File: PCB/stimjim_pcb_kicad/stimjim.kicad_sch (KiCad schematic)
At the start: 41 parts, among them J1 Conn_02x08_Odd_Even, J10 USB4105-GF-A, J11 BM03B-SRSS-TB, J4 10129383-910002ALF, SW1 400MSP1R6BLKM6QE, U151 AP2112K-3.3

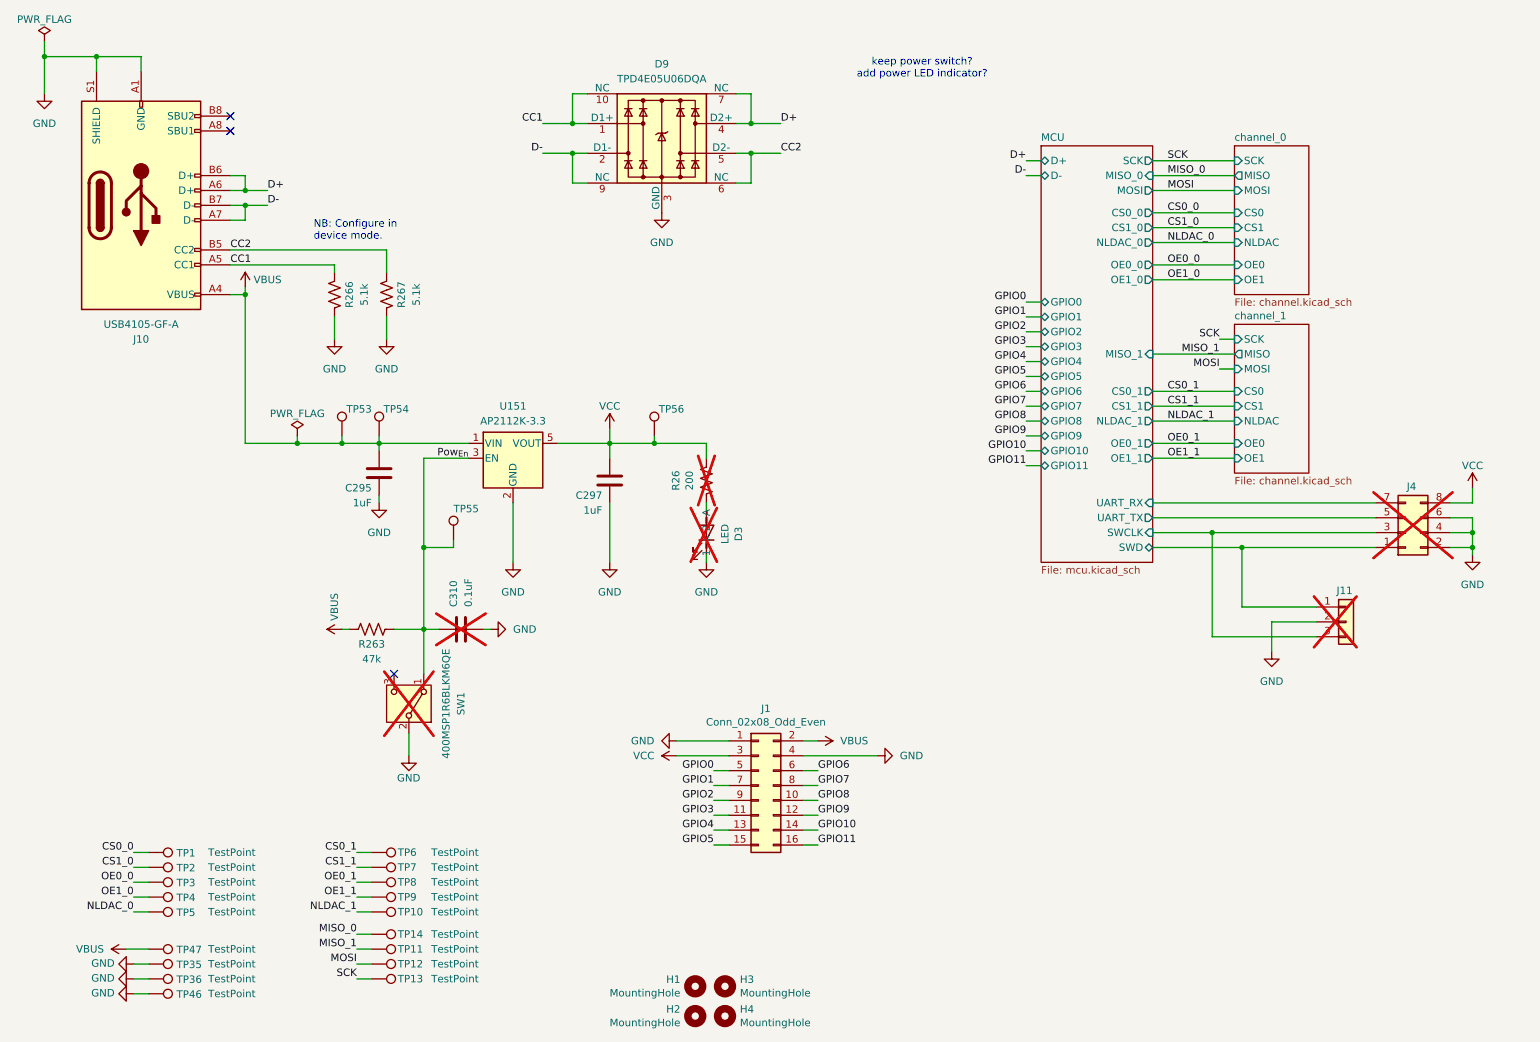
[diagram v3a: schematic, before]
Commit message: Simplified layout
- Went to 4 layers
- Simplified GPIO interface and remove power connections since they are
  a recipe for disaster
- Independent SPI busses to each stimulator to allow simultaneous
  control
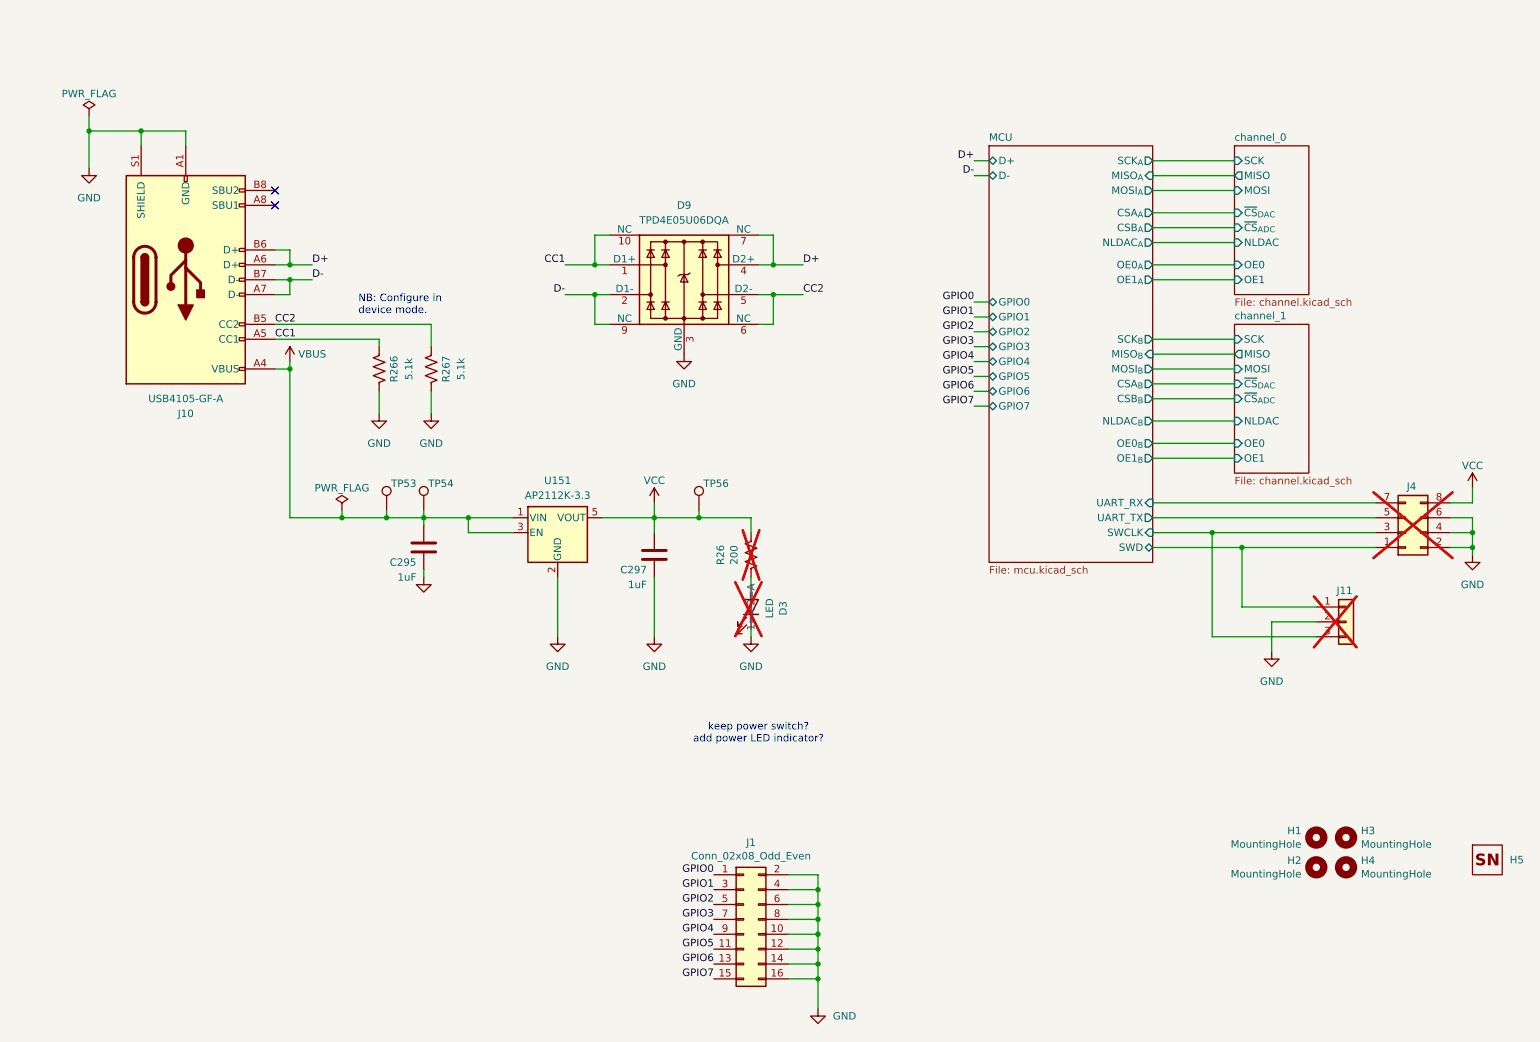
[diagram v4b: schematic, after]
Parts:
- removed C310: 0.1uF, Capacitor_SMD:C_0402_1005Metric, symbol Device:C
- removed R263: 47k, Resistor_SMD:R_0402_1005Metric, symbol Device:R_US
- removed SW1: 400MSP1R6BLKM6QE, Button_Switch_THT:SW_Push_2P2T_Vertical_E-Switch_800UDP8P1A1M6, symbol Switch:SW_SPDT
- removed TP1, TP10, TP11, TP12, TP13, TP14, TP2, TP3, TP35, TP36, TP4, TP46, TP47, TP5, TP6, TP7, TP8, TP9: TestPoint, TestPoint:TestPoint_THTPad_D1.0mm_Drill0.5mm, symbol Connector:TestPoint
- removed TP55: GND, TestPoint:TestPoint_Pad_D2.0mm, symbol Connector:TestPoint
- added H5: ~, open-ephys:OEPS_SN-STICKER-8x20mm, symbol open-ephys:OEPS-SN
- J10: footprint Connector_USB:USB_C_Receptacle_GCT_USB4105-xx-A_16P_TopMnt_Horizontal -> open-ephys:USB_C_Receptacle_GCT_USB4105-xx-A_16P_TopMnt_Horizontal
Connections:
- net GPIO10 is gone; now on net GND: J1.14 (Pin_14)
- net GPIO11 is gone; now on net GND: J1.16 (Pin_16)
- net GPIO8 is gone; now on net GND: J1.10 (Pin_10)
- net GPIO9 is gone; now on net GND: J1.12 (Pin_12)
- net Pow_{En} is gone; now on net VBUS: U151.3 (EN)
- net GND: now also J1.2 (Pin_2), J1.6 (Pin_6), J1.8 (Pin_8); no longer J1.1 (Pin_1)
- net GPIO0: now also J1.1 (Pin_1); no longer J1.5 (Pin_5)
- net GPIO1: now also J1.3 (Pin_3); no longer J1.7 (Pin_7)
- net GPIO2: now also J1.5 (Pin_5); no longer J1.9 (Pin_9)
- net GPIO3: now also J1.7 (Pin_7); no longer J1.11 (Pin_11)
- net GPIO4: now also J1.9 (Pin_9); no longer J1.13 (Pin_13)
- net GPIO5: now also J1.11 (Pin_11); no longer J1.15 (Pin_15)
- net GPIO6: now also J1.13 (Pin_13); no longer J1.6 (Pin_6)
- net GPIO7: now also J1.15 (Pin_15); no longer J1.8 (Pin_8)
- net VBUS: no longer J1.2 (Pin_2)
- net VCC: no longer J1.3 (Pin_3)
- no-connect marks 3 -> 2
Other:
- sheet MCU ports: added CSA_{A}, CSA_{B}, CSB_{A}, CSB_{B}, MISO_{A}, MISO_{B}, MOSI_{A}, MOSI_{B}, NLDAC_{A}, NLDAC_{B}, OE0_{A}, OE0_{B}, OE1_{A}, OE1_{B}, SCK_{A}, SCK_{B}; removed CS0_0, CS0_1, CS1_0, CS1_1, GPIO10, GPIO11, GPIO8, GPIO9, MISO_0, MISO_1, MOSI, NLDAC_0, NLDAC_1, OE0_0, OE0_1, OE1_0, OE1_1, SCK
- sheet channel_0 ports: added ~{CS}_{ADC}, ~{CS}_{DAC}; removed CS0, CS1
- sheet channel_1 ports: added ~{CS}_{ADC}, ~{CS}_{DAC}; removed CS0, CS1
- title: stimjim -> StimJim
- moved on the sheet: C295, C297, D3, D9, H1, H2, H3, H4, J1, J10, R26, R266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

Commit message: filipe feedback
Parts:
- D3, R26: now fitted
- J1: footprint microstim:Multicomp_MC9A22-1634_2x08x2.54mm_Angled -> Connector_IDC:IDC-Header_2x08_P2.54mm_Horizontal
- J10: footprint open-ephys:USB_C_Receptacle_GCT_USB4105-xx-A_16P_TopMnt_Horizontal -> Connector_USB:USB_C_Receptacle_GCT_USB4105-xx-A_16P_TopMnt_Horizontal
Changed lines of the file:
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@@
 			)
 		)
-		(property "Footprint" "microstim:Multicomp_MC9A22-1634_2x08x2.54mm_Angled"
+		(property "Footprint" "Connector_IDC:IDC-Header_2x08_P2.54mm_Horizontal"
 			(at 139.7 170.18 0)
 			(effects
@@
 		(in_bom no)
 		(on_board yes)
-		(dnp yes)
+		(dnp no)
 		(property "Reference" "D3"
 			(at 146.4564 117.0686 0)
@@
 			)
 		)
-		(property "Footprint" "open-ephys:USB_C_Receptacle_GCT_USB4105-xx-A_16P_TopMnt_Horizontal"
+		(property "Footprint" "Connector_USB:USB_C_Receptacle_GCT_USB4105-xx-A_16P_TopMnt_Horizontal"
 			(at 48.26 60.96 0)
 			(effects
@@
 		(in_bom no)
 		(on_board yes)
-		(dnp yes)
+		(dnp no)
 		(property "Reference" "R26"
 			(at 135.763 107.95 90)
